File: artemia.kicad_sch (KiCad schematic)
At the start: 0 parts

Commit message: WIP
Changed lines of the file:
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@@
     )
     (instances
-      (project "prototype"
+      (project "artemia"
         (path "/3ef271cf-72c1-43e9-bc06-d7d78e288e38" (page "2"))
       )
@@
       (effects (font (size 1.27 1.27)) (justify left))
     )
-    (pin "V_{3.3}" input (at 191.77 125.73 0)
+    (pin "V_{3.3}" output (at 191.77 125.73 0)
       (effects (font (size 1.27 1.27)) (justify right))
     )
@@
       (effects (font (size 1.27 1.27)) (justify right))
     )
-    (pin "V_{ADP_SENSE_EN}" input (at 191.77 147.32 0)
+    (pin "V_{ADP_SENSE_EN}" output (at 191.77 147.32 0)
       (effects (font (size 1.27 1.27)) (justify right))
     )
-    (pin "V_{RTC_SENSE_EN}" input (at 191.77 140.97 0)
+    (pin "V_{RTC_SENSE_EN}" output (at 191.77 140.97 0)
       (effects (font (size 1.27 1.27)) (justify right))
     )
-    (pin "SHD" input (at 191.77 134.62 0)
+    (pin "SHD" output (at 191.77 134.62 0)
       (effects (font (size 1.27 1.27)) (justify right))
     )
-    (pin "FORCE_ON" input (at 191.77 137.16 0)
+    (pin "FORCE_ON" output (at 191.77 137.16 0)
       (effects (font (size 1.27 1.27)) (justify right))
     )
@@
     )
     (instances
-      (project "prototype"
+      (project "artemia"
         (path "/3ef271cf-72c1-43e9-bc06-d7d78e288e38" (page "5"))
       )
@@
       (effects (font (size 1.27 1.27)) (justify right))
     )
-    (pin "V_{ADP_SENSE}" input (at 191.77 97.79 0)
+    (pin "V_{ADP_SENSE}" output (at 191.77 97.79 0)
       (effects (font (size 1.27 1.27)) (justify right))
     )
@@
       (effects (font (size 1.27 1.27)) (justify right))
     )
-    (pin "V_{RTC_SENSE}" input (at 191.77 92.71 0)
+    (pin "V_{RTC_SENSE}" output (at 191.77 92.71 0)
       (effects (font (size 1.27 1.27)) (justify right))
     )
@@
     )
     (instances
-      (project "prototype"
+      (project "artemia"
         (path "/3ef271cf-72c1-43e9-bc06-d7d78e288e38" (page "3"))
       )
@@
       (effects (font (size 1.27 1.27)) (justify left top))
     )
-    (pin "ALARM" input (at 139.7 58.42 180)
+    (pin "ALARM" output (at 139.7 58.42 180)
       (effects (font (size 1.27 1.27)) (justify left))
     )
@@
       (effects (font (size 1.27 1.27)) (justify right))
     )
-    (pin "V_{RTC}" input (at 139.7 44.45 180)
+    (pin "V_{RTC}" output (at 139.7 44.45 180)
       (effects (font (size 1.27 1.27)) (justify left))
     )
@@
     )
     (instances
-      (project "prototype"
+      (project "artemia"
         (path "/3ef271cf-72c1-43e9-bc06-d7d78e288e38" (page "4"))
       )

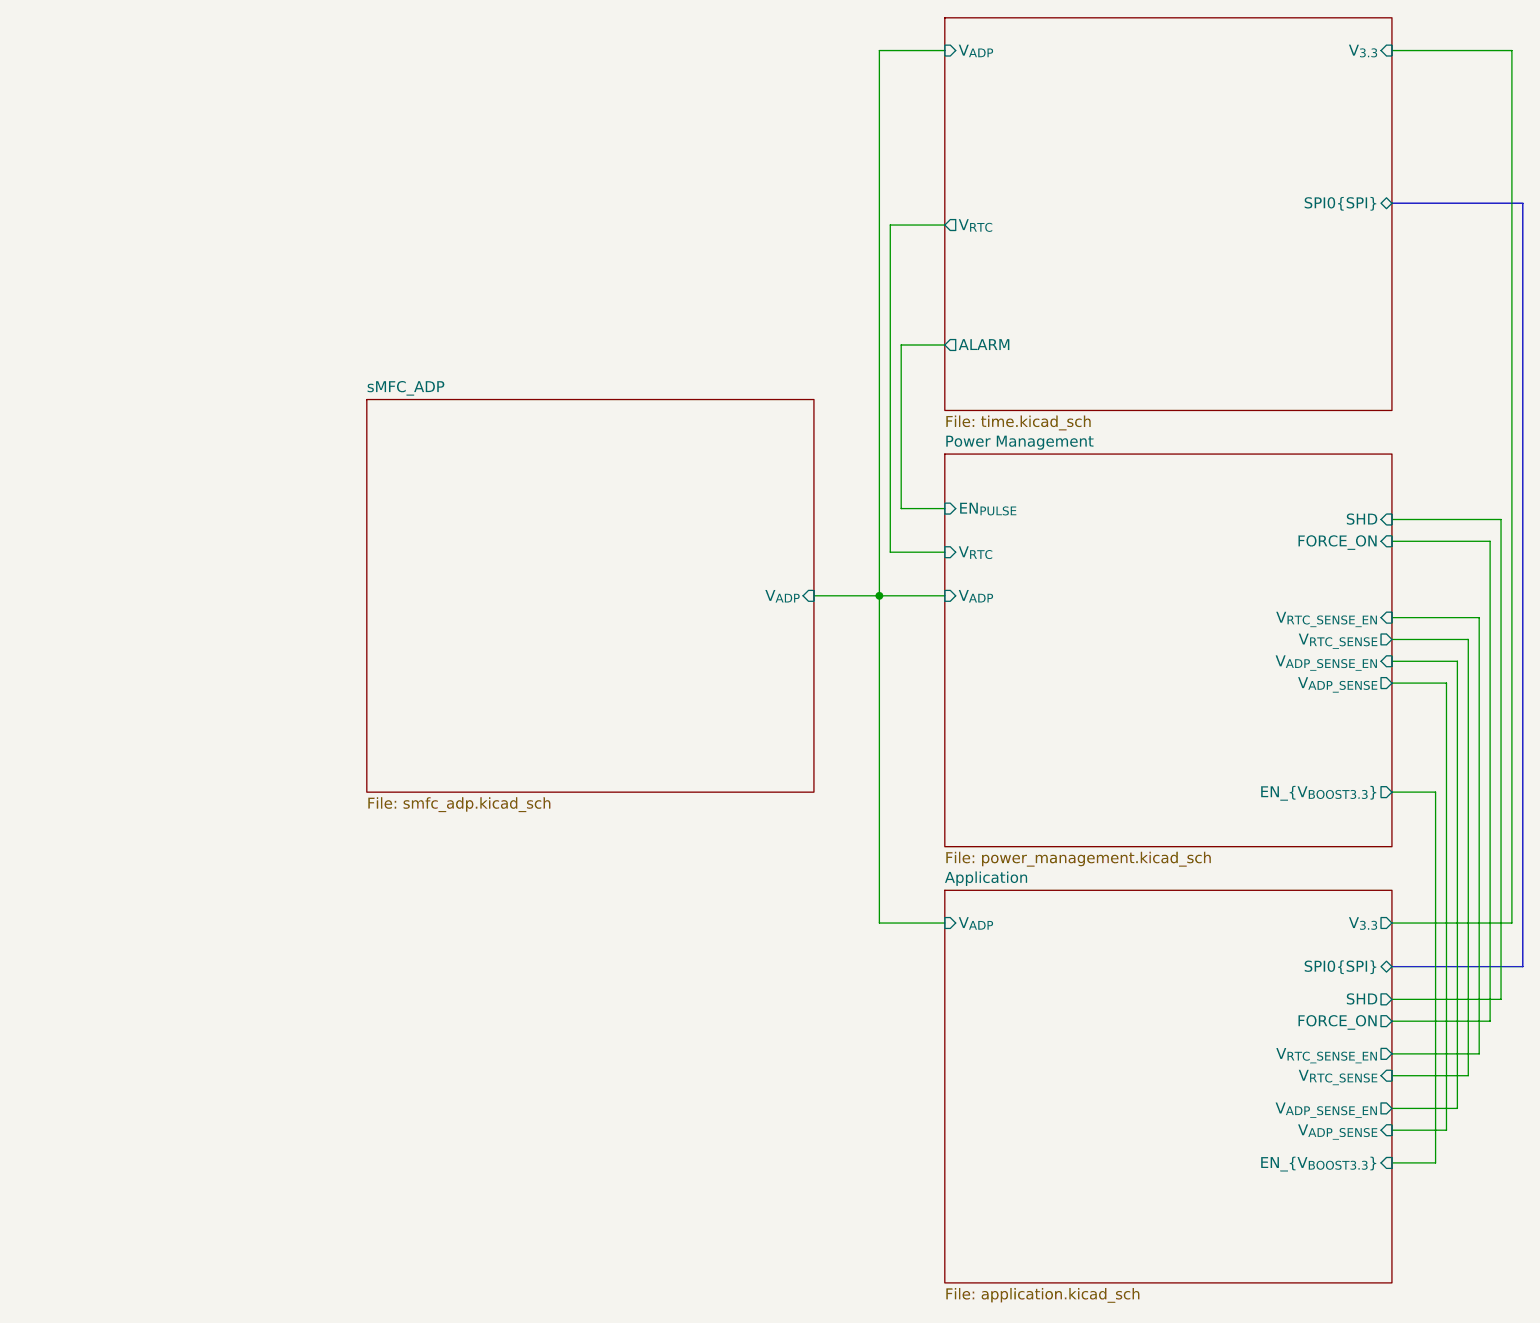
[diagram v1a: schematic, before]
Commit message: Added LoRa module, lots of fixes & tweaks
 - Added loRa module as last Artemia experiment uses LoRa RFM95W
 - Added headers for debuggging purposes
 - Expanded board size to account for added hardware
 - Updated clearances to match JLCPCB manufacturing capabilities (I
   figure that if JLCPCB can fab it, anyone else can)
 - Fixed DRC issues (still need to run analysis on schematic)
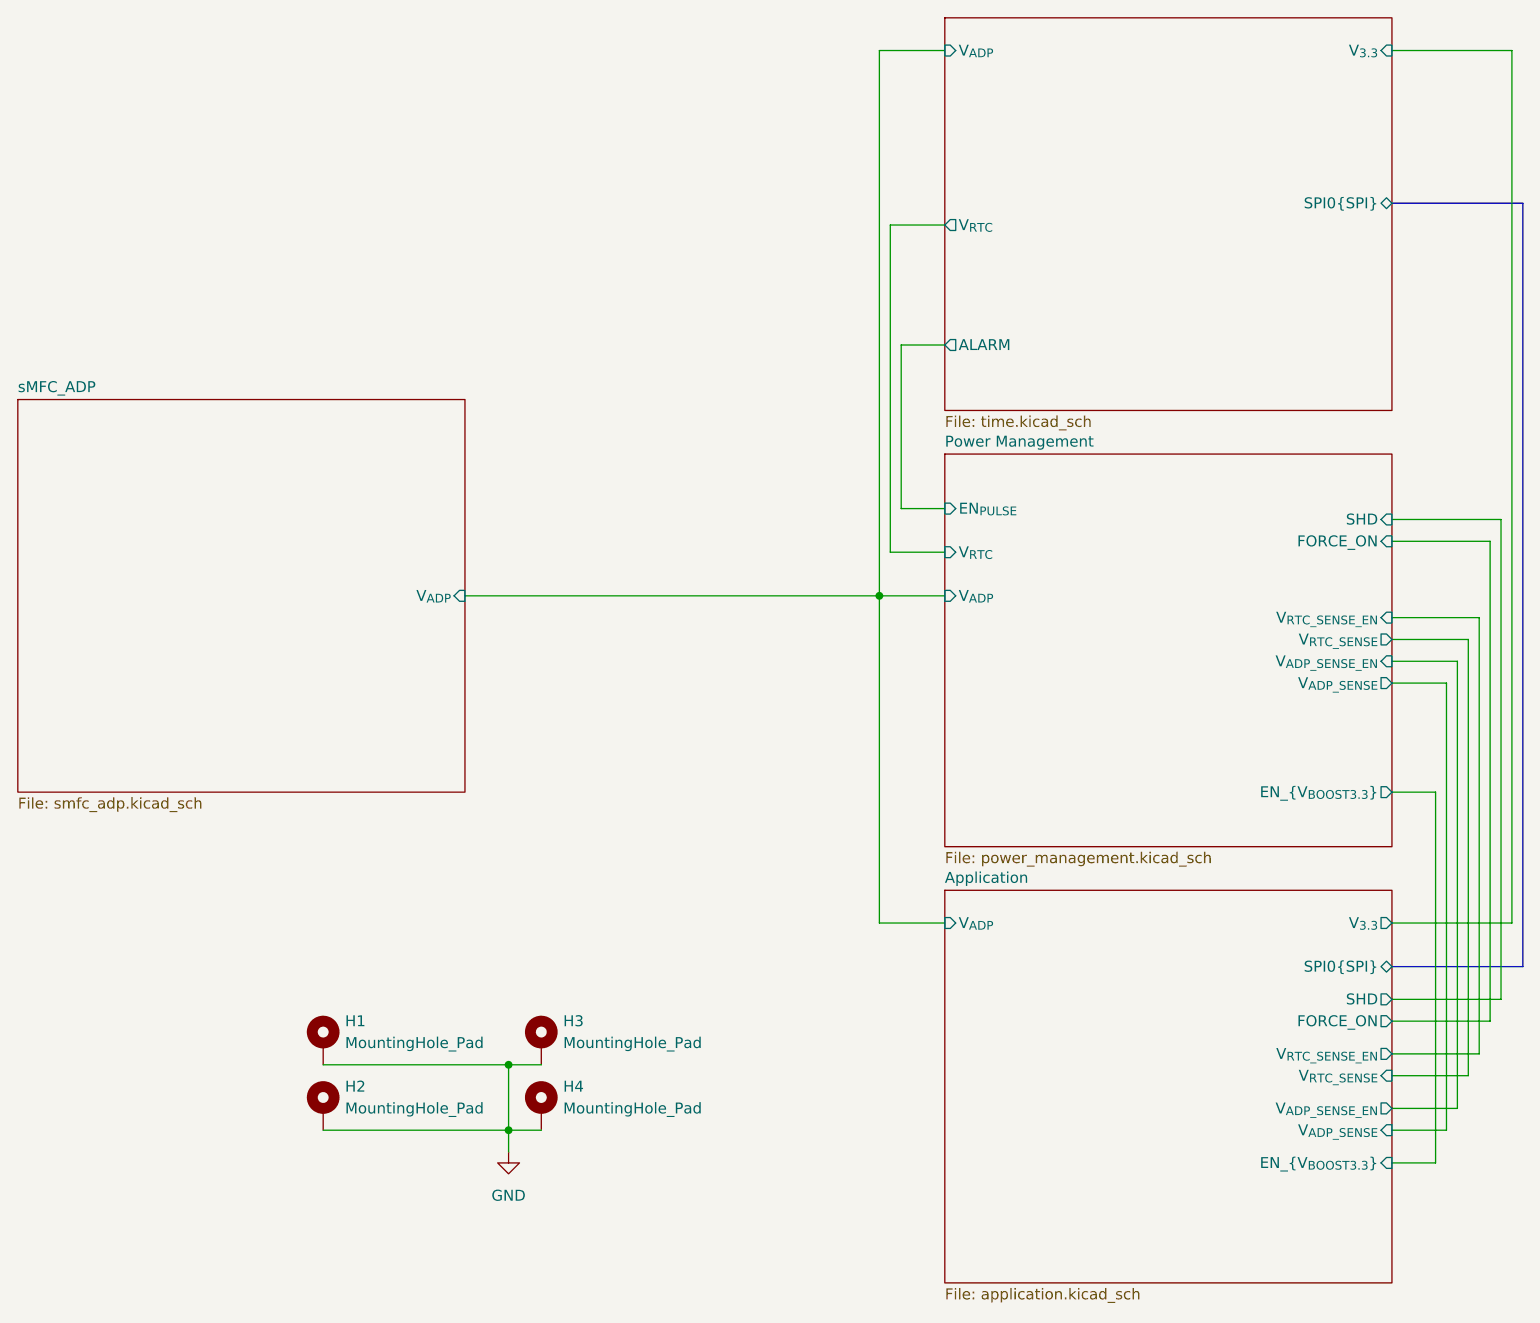
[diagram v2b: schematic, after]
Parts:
- added H1, H2, H3, H4: MountingHole_Pad, MountingHole:MountingHole_3.2mm_M3_Pad_Via, symbol Mechanical:MountingHole_Pad
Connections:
- new net GND: H1.1, H2.1, H3.1, H4.1
